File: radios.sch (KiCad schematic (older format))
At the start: 4 parts, among them J8 CONN_8X2, J9 CONN_6X2

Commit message: Continued syncing with original design.
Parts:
- F29: renamed from F?; value FUSE -> 1.1A 5V; Digikey (none) -> F3366CT-ND
- F30: renamed from F?; value FUSE -> 1.5A 5V; Digikey (none) -> F3367CT-ND
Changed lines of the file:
@@
 $Descr A4 11693 8268
 encoding utf-8
-Sheet 3 6
+Sheet 3 9
 Title ""
-Date "14 aug 2015"
+Date "21 aug 2015"
 Rev ""
 Comp ""
@@
 	4100 1550 4000 1550
 $Comp
-L GND #PWR?
+L GND #PWR029
 U 1 1 55CD562D
 P 3100 1450
-F 0 "#PWR?" H 3100 1450 30  0001 C CNN
+F 0 "#PWR029" H 3100 1450 30  0001 C CNN
 F 1 "GND" H 3100 1380 30  0001 C CNN
 F 2 "" H 3100 1450 60  0000 C CNN
@@
 $EndComp
 Wire Bus Line
-	2850 1200 2850 1450
-Wire Bus Line
-	2850 1450 2850 1650
-Wire Bus Line
-	2850 1650 2850 1750
-Wire Bus Line
-	2850 1750 2850 1850
+	2850 1200 2850 1850
 Entry Wire Line
 	2850 1450 2950 1550
@@
 	3200 1450 3100 1450
 $Comp
-L +5V #PWR?
+L +5V #PWR030
 U 1 1 55CD566E
 P 3000 700
-F 0 "#PWR?" H 3000 790 20  0001 C CNN
+F 0 "#PWR030" H 3000 790 20  0001 C CNN
 F 1 "+5V" H 3000 790 30  0000 C CNN
 F 2 "" H 3000 700 60  0000 C CNN
@@
 $EndComp
 $Comp
-L FUSE F?
+L FUSE F30
 U 1 1 55CD5687
 P 3000 1050
-F 0 "F?" H 3100 1100 40  0000 C CNN
-F 1 "FUSE" H 2900 1000 40  0000 C CNN
+F 0 "F30" H 3100 1100 40  0000 C CNN
+F 1 "1.5A 5V" H 2900 1000 40  0000 C CNN
 F 2 "~" H 3000 1050 60  0000 C CNN
 F 3 "~" H 3000 1050 60  0000 C CNN
+F 4 "F3367CT-ND" H 3000 1050 60  0001 C CNN "Digikey"
 	1    3000 1050
 	0    -1   -1   0
@@
 RCTS
 $Comp
-L FUSE F?
+L FUSE F29
 U 1 1 55CD5DFF
 P 1000 1150
-F 0 "F?" H 1100 1200 40  0000 C CNN
-F 1 "FUSE" H 900 1100 40  0000 C CNN
+F 0 "F29" H 1100 1200 40  0000 C CNN
+F 1 "1.1A 5V" H 900 1100 40  0000 C CNN
 F 2 "~" H 1000 1150 60  0000 C CNN
 F 3 "~" H 1000 1150 60  0000 C CNN
+F 4 "F3366CT-ND" H 1000 1150 60  0001 C CNN "Digikey"
 	1    1000 1150
 	0    -1   -1   0
 $EndComp
 $Comp
-L +5V #PWR?
+L +5V #PWR031
 U 1 1 55CD5E05
 P 1000 750
-F 0 "#PWR?" H 1000 840 20  0001 C CNN
+F 0 "#PWR031" H 1000 840 20  0001 C CNN
 F 1 "+5V" H 1000 840 30  0000 C CNN
 F 2 "" H 1000 750 60  0000 C CNN
@@
 $EndComp
 $Comp
-L GND #PWR?
+L GND #PWR032
 U 1 1 55CD5E0B
 P 1150 2150
-F 0 "#PWR?" H 1150 2150 30  0001 C CNN
+F 0 "#PWR032" H 1150 2150 30  0001 C CNN
 F 1 "GND" H 1150 2080 30  0001 C CNN
 F 2 "" H 1150 2150 60  0000 C CNN

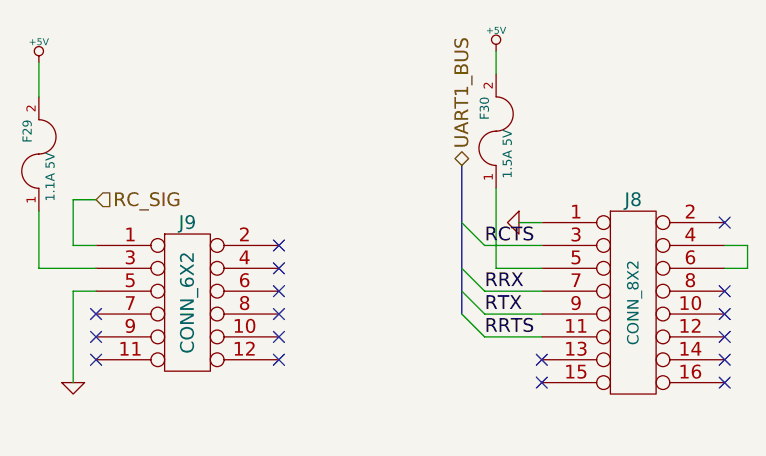
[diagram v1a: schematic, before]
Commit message: Finishing bom integration with schematic.
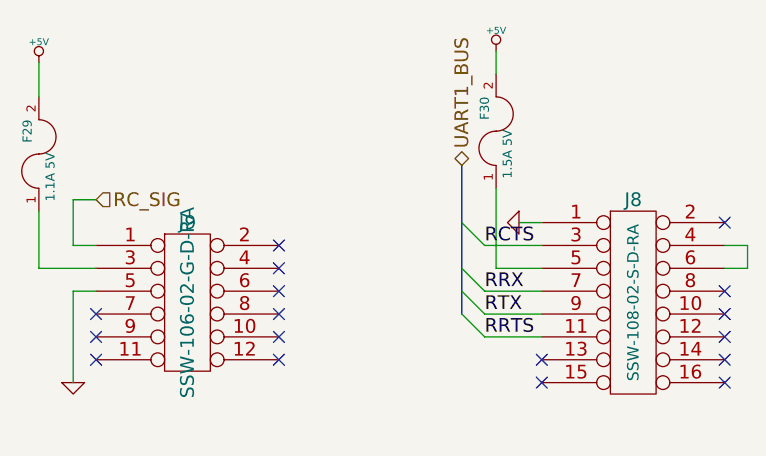
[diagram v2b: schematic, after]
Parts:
- J8: value CONN_8X2 -> SSW-108-02-S-D-RA; footprint (none) -> ~
- J9: value CONN_6X2 -> SSW-106-02-G-D-RA; footprint (none) -> ~
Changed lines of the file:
@@
 LIBS:p_samtec
 LIBS:w_transistor
+LIBS:w_analog
 LIBS:distro-cache
 EELAYER 27 0
@@
 Sheet 3 9
 Title ""
-Date "21 aug 2015"
+Date "22 aug 2015"
 Rev ""
 Comp ""
@@
 P 1650 1800
 F 0 "J9" H 1650 2150 60  0000 C CNN
-F 1 "CONN_6X2" V 1650 1800 60  0000 C CNN
-F 2 "" H 1650 1800 60  0000 C CNN
-F 3 "" H 1650 1800 60  0000 C CNN
+F 1 "SSW-106-02-G-D-RA" V 1650 1800 60  0000 C CNN
+F 2 "~" H 1650 1800 60  0000 C CNN
+F 3 "~" H 1650 1800 60  0000 C CNN
 	1    1650 1800
 	1    0    0    -1
@@
 P 3600 1800
 F 0 "J8" H 3600 2250 60  0000 C CNN
-F 1 "CONN_8X2" V 3600 1800 50  0000 C CNN
-F 2 "" H 3600 1800 60  0000 C CNN
-F 3 "" H 3600 1800 60  0000 C CNN
+F 1 "SSW-108-02-S-D-RA" V 3600 1800 50  0000 C CNN
+F 2 "~" H 3600 1800 60  0000 C CNN
+F 3 "~" H 3600 1800 60  0000 C CNN
 	1    3600 1800
 	1    0    0    -1
